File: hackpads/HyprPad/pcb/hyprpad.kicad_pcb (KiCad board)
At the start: 2 copper layers, 45 x 100 mm, 7 parts, among them U1 MCU_Seeed_XIAO_RP2040

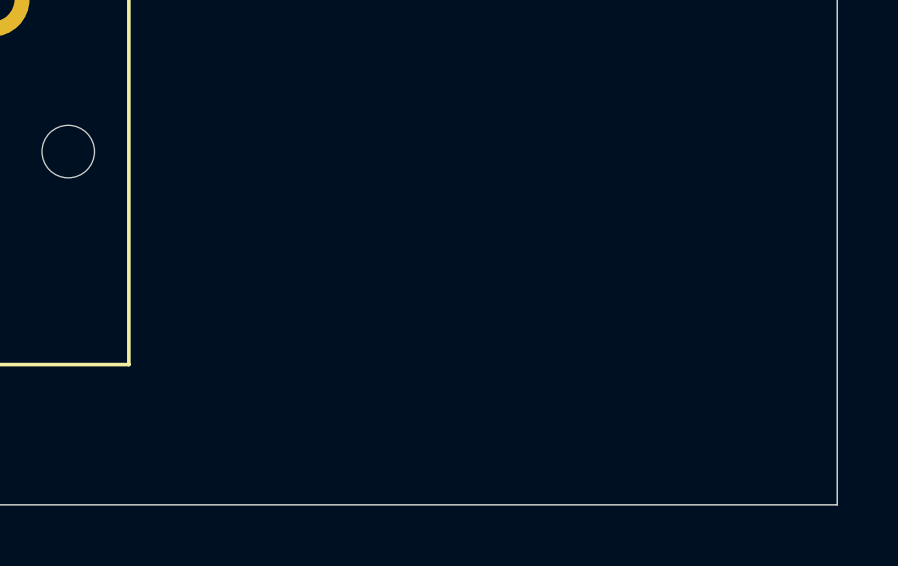
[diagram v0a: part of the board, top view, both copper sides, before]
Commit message: add orpheus
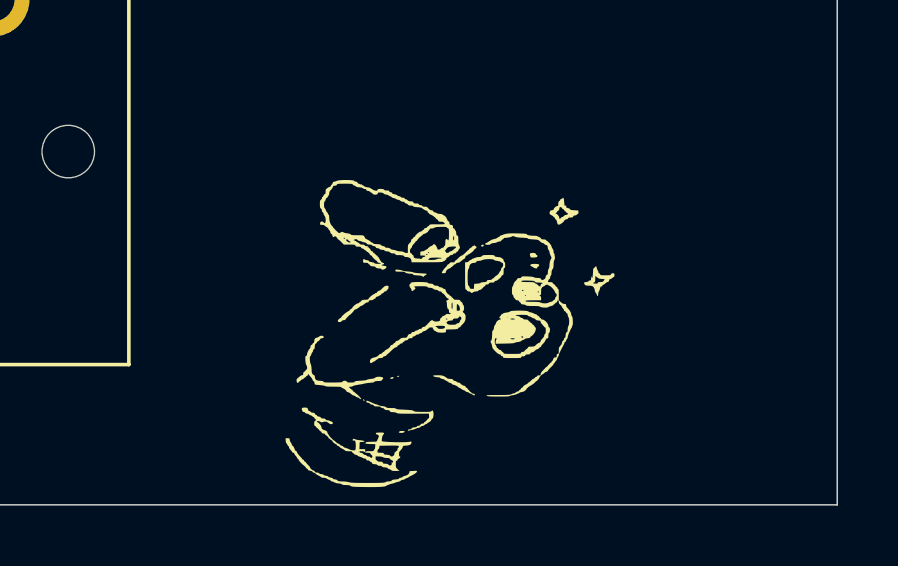
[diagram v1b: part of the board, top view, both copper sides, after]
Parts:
- added G***: LOGO, LOGO, F.Cu at (108.2, 144.3)
- added G***: LOGO, LOGO, B.Cu at (98.1, 62.3)

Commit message: new gerber
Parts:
- added G***: LOGO, LOGO, B.Cu at (115.8, 124.6)
- added G***: LOGO, LOGO, B.Cu at (114.8, 108.1)
- added G***: LOGO, LOGO, B.Cu at (100.9, 135.4)
- moved G*** 25.5 mm to (106.2, 86.5)

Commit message: update PCB
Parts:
- moved U1 1.96 mm to (110.3, 60.1)
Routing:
- net Net-(U1-PB08_A6_D6_TX): track 72.6 -> 91.6 mm, vias 2 -> 1
- net GND: track 103.7 -> 112.1 mm
- net Net-(U1-PA6_A10_D10_MOSI): track 32.0 -> 39.5 mm, vias 0 -> 2
- net Net-(U1-PA7_A8_D8_SCK): track 45.7 -> 48.8 mm
- net Net-(U1-PA5_A9_D9_MISO): track 36.5 -> 38.0 mm
- net Net-(U1-PB09_A7_D7_RX): track 61.3 -> 61.6 mm, vias 0 -> 1
